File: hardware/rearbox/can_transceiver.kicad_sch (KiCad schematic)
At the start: 9 parts, among them U5 MCP2542FD

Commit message: Changed power section
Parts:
- renumbered D2 to D1, R8 to R7
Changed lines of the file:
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@@
 (kicad_sch
-	(version 20231120)
+	(version 20250114)
 	(generator "eeschema")
-	(generator_version "8.0")
+	(generator_version "9.0")
 	(paper "A4")
 	(title_block
@@
 		(shape output)
 		(at 123.19 105.41 180)
-		(fields_autoplaced yes)
 		(effects
 			(font
@@
 		(shape input)
 		(at 123.19 102.87 180)
-		(fields_autoplaced yes)
 		(effects
 			(font
@@
 		(shape bidirectional)
 		(at 177.8 118.11 0)
-		(fields_autoplaced yes)
 		(effects
 			(font
@@
 		(shape bidirectional)
 		(at 177.8 97.79 0)
-		(fields_autoplaced yes)
 		(effects
 			(font
@@
 		(on_board yes)
 		(dnp no)
-		(property "Reference" "D2"
+		(property "Reference" "D1"
 			(at 163.83 109.22 0)
 			(effects
@@
 		(dnp no)
 		(fields_autoplaced yes)
-		(property "Reference" "#FLG014"
+		(property "Reference" "#FLG012"
 			(at 149.225 81.28 0)
 			(effects
@@
 		(dnp no)
 		(fields_autoplaced yes)
-		(property "Reference" "#FLG013"
+		(property "Reference" "#FLG011"
 			(at 130.175 81.28 0)
 			(effects
@@
 		(on_board yes)
 		(dnp no)
-		(property "Reference" "R8"
+		(property "Reference" "R7"
 			(at 125.73 115.57 0)
 			(effects

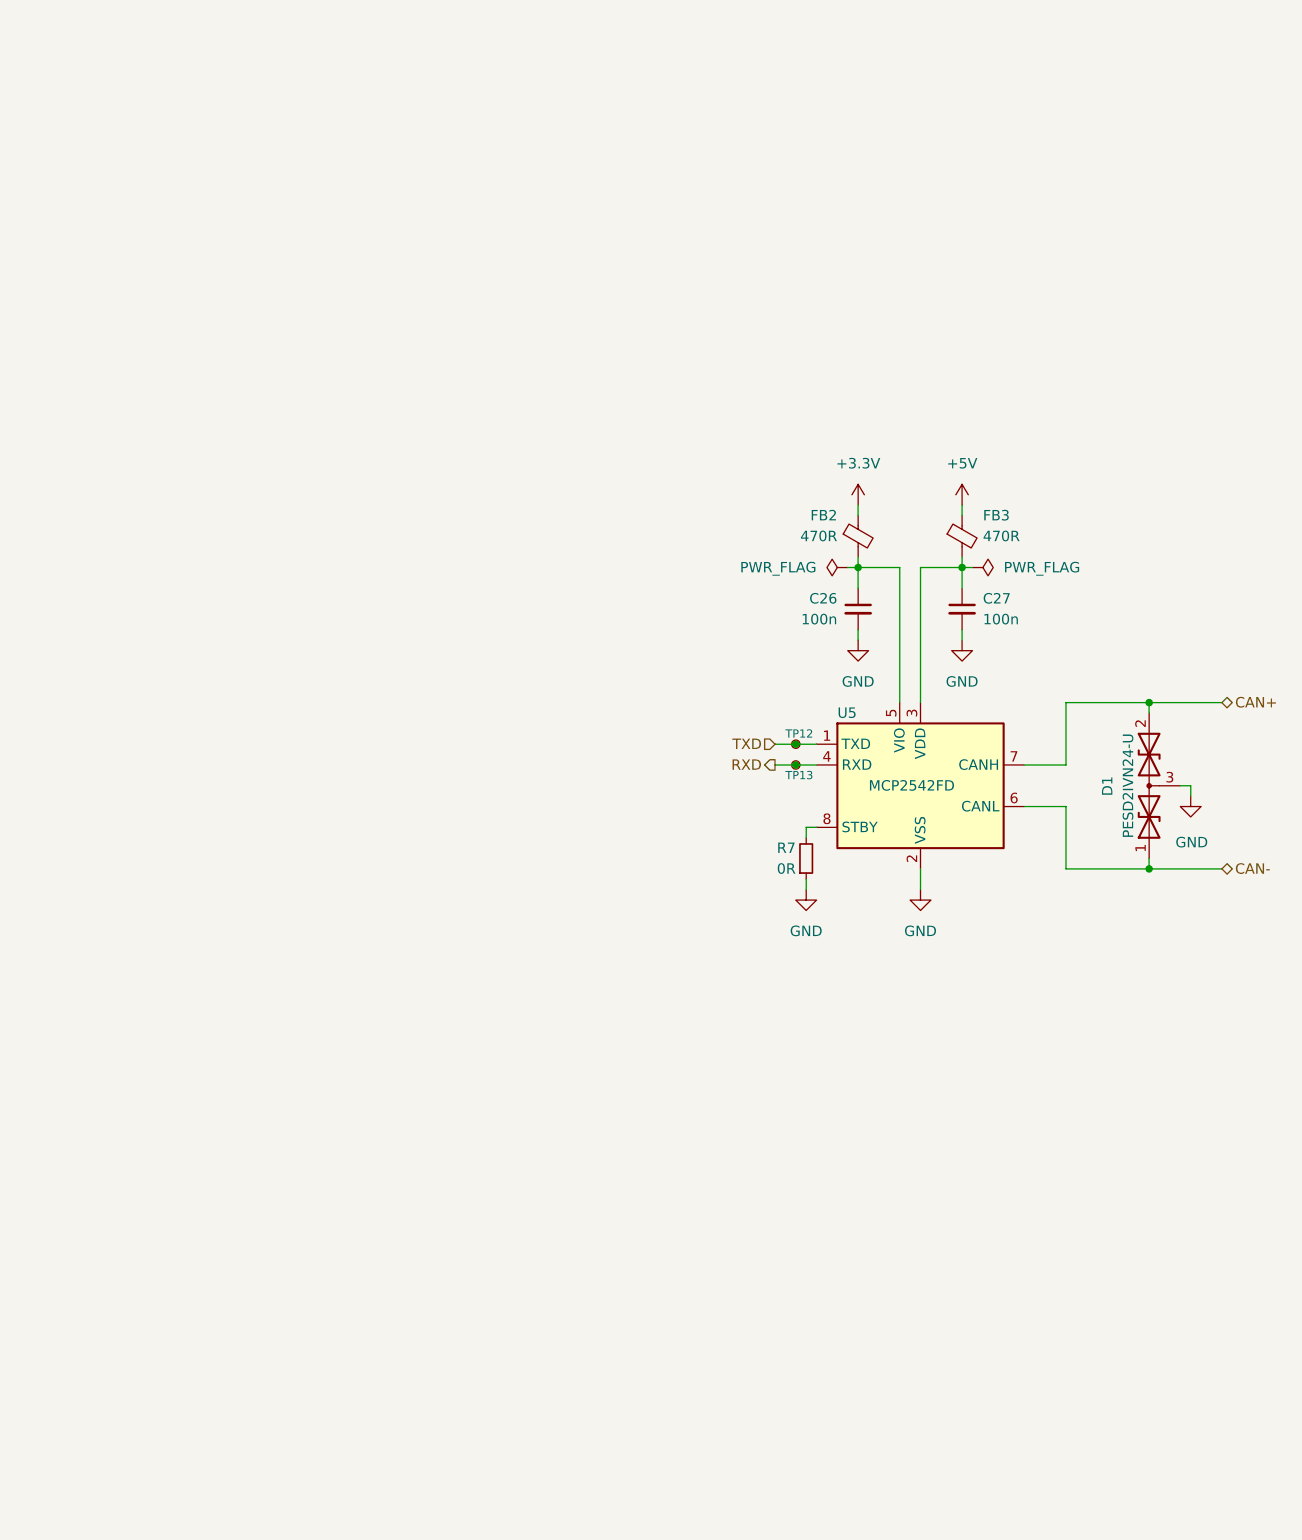
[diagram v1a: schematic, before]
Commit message: Deleted measurement systems for new iteration
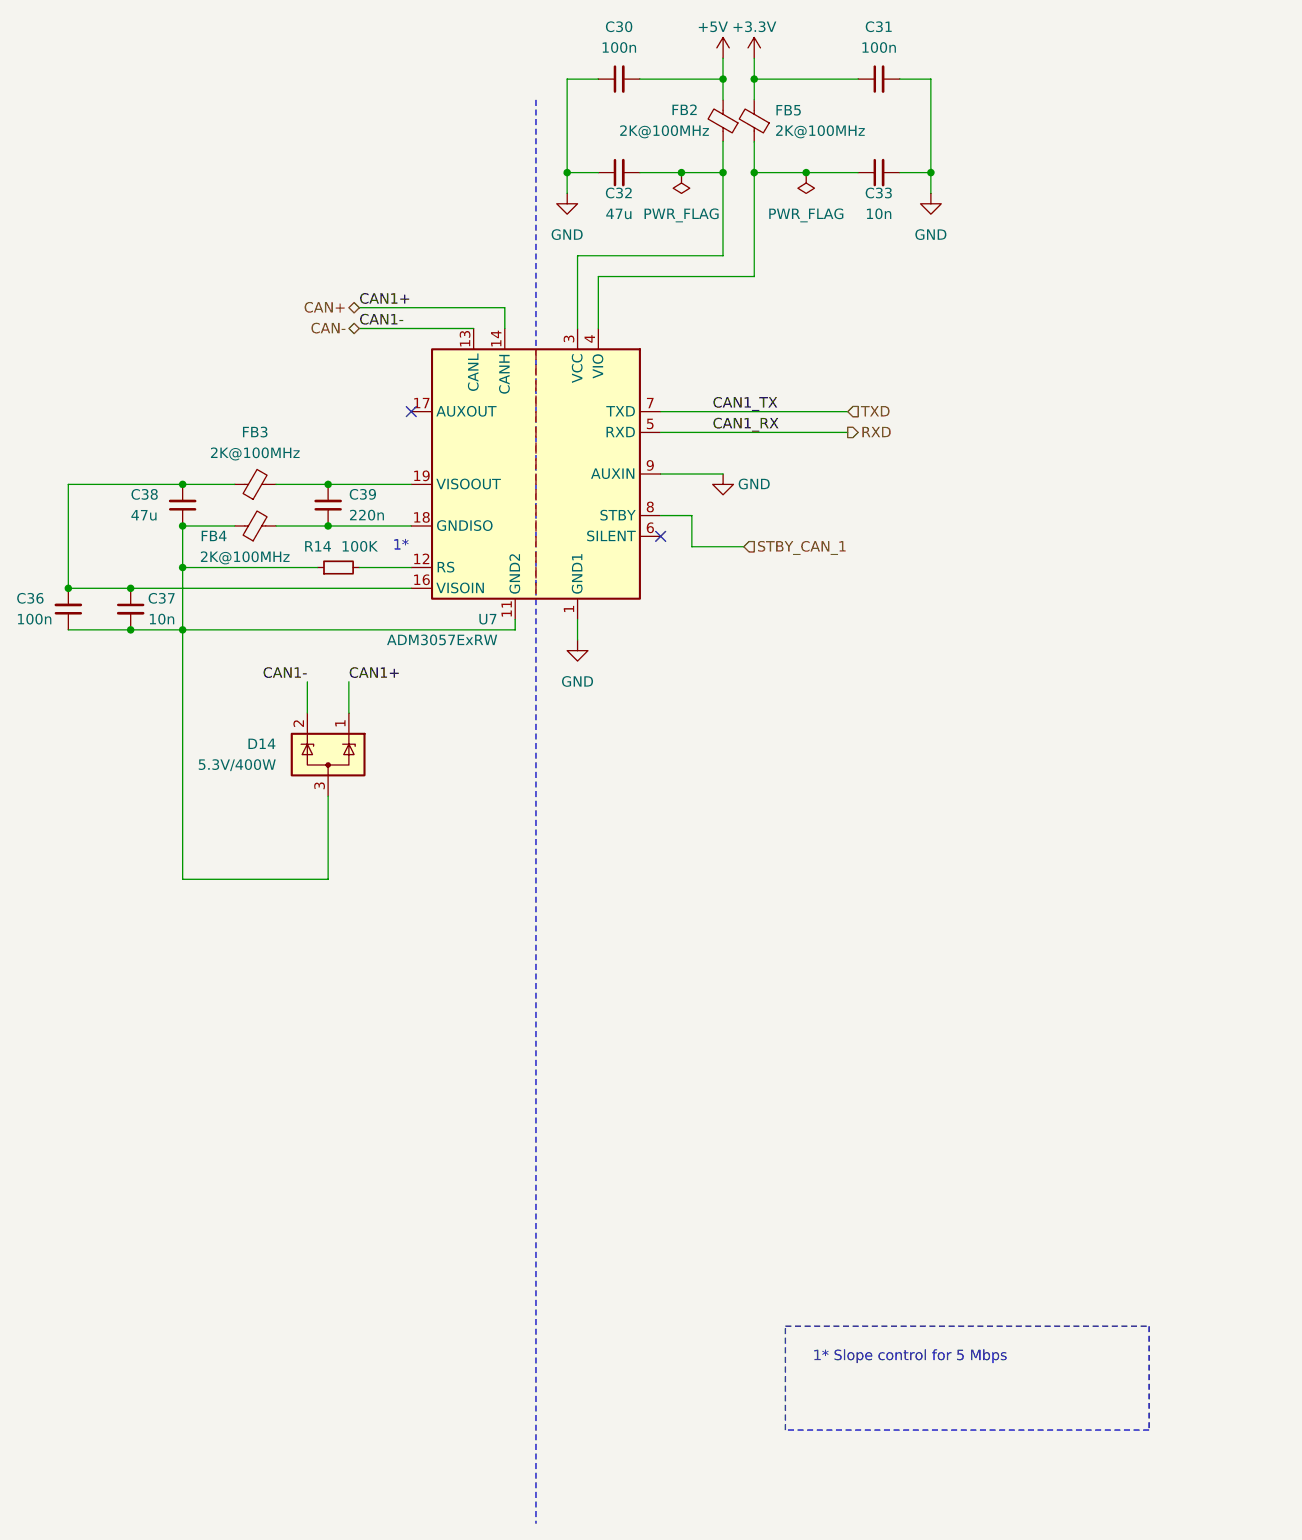
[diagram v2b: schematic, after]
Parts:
- removed C26, C27: 100n, Capacitor_SMD:C_0603_1608Metric, symbol Device:C_Small
- removed D1: PESD2IVN24-U, Package_TO_SOT_SMD:SOT-323_SC-70, symbol Device:D_TVS_Dual_AAC
- removed R7: 0R, Resistor_SMD:R_0603_1608Metric, symbol Device:R_Small
- removed TP12, TP13: TestPoint_Small, TestPoint:TestPoint_Pad_D1.0mm, symbol Connector:TestPoint_Small
- removed U5: MCP2542FD, Package_DFN_QFN:DFN-8-1EP_3x3mm_P0.65mm_EP1.55x2.4mm, symbol Interface_CAN_LIN:MCP2542FDxMF
- added C30, C31, C36: 100n, Capacitor_SMD:C_0603_1608Metric_Pad1.08x0.95mm_HandSolder, symbol Device:C_Small
- added C32, C38: 47u, Capacitor_SMD:C_0603_1608Metric_Pad1.08x0.95mm_HandSolder, symbol Device:C_Small
- added C33, C37: 10n, Capacitor_SMD:C_0603_1608Metric_Pad1.08x0.95mm_HandSolder, symbol Device:C_Small
- added C39: 220n, Capacitor_SMD:C_0603_1608Metric_Pad1.08x0.95mm_HandSolder, symbol Device:C_Small
- added D14: 5.3V/400W, Package_TO_SOT_SMD:SOT-23-3, symbol Power_Protection:ESDA5V3L
- added FB4, FB5: 2K@100MHz, Inductor_SMD:L_0603_1608Metric_Pad1.05x0.95mm_HandSolder, symbol Device:FerriteBead_Small
- added R14: 100K, Resistor_SMD:R_0603_1608Metric_Pad0.98x0.95mm_HandSolder, symbol Device:R_Small
- added U7: ADM3057ExRW, Package_SO:SOIC-20W_7.5x12.8mm_P1.27mm, symbol Interface_CAN_LIN:ADM3057ExRW
- FB2, FB3: value 470R -> 2K@100MHz; footprint Inductor_SMD:L_0603_1608Metric -> Inductor_SMD:L_0603_1608Metric_Pad1.05x0.95mm_HandSolder
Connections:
- net +3.3V: now also C31.1, FB5.2; no longer FB2.1
- net +5V: now also FB2.2, C30.2; no longer FB3.1
- net CAN+: now also D14.1 (K), U7.14 (CANH)
- net CAN-: now also D14.2 (K), U7.13 (CANL)
- net GND: now also C30.1, C31.2, C32.1, C33.2, U7.1 (GND1), U7.10 (GND1), U7.2 (GND1), U7.9 (AUXIN)
- net RXD: now also U7.5 (RXD)
- net TXD: now also U7.7 (TXD)
- net at FB3.2: now also C39.2, U7.19 (VISOOUT)
- new net: C36.1, C37.2, C38.1, D14.3 (A), FB4.1, R14.1, U7.11 (GND2), U7.15 (GND2)
- new net: C39.1, FB4.2, U7.18 (GNDISO), U7.20 (GNDISO)
- new net: C32.2, FB2.1, U7.3 (VCC)
- new net: R14.2, U7.12 (RS)
- new net: C36.2, C37.1, C38.2, FB3.1, U7.16 (VISOIN)
- new net: C33.1, FB5.1, U7.4 (VIO)
- new net STBY_CAN_1: U7.8 (STBY)
- no-connect marks 0 -> 2
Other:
- note added: "1*"
- note added: "1* Slope control for 5 Mbps"

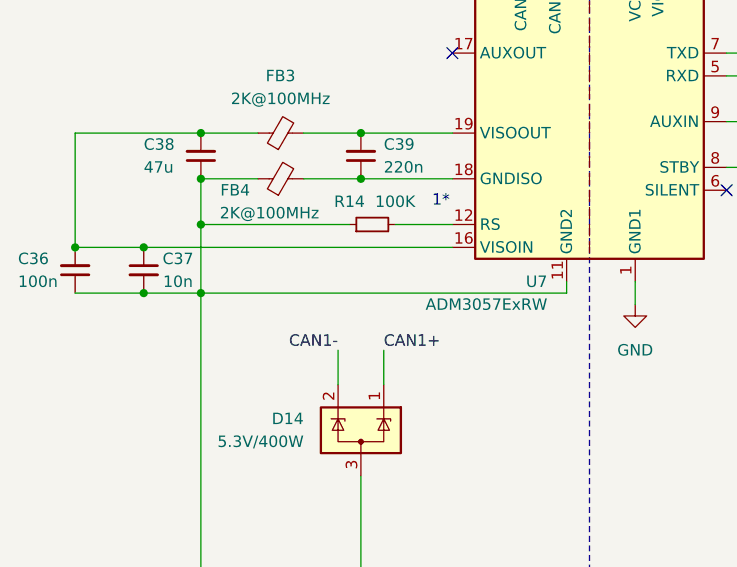
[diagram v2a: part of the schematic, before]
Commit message: Fixed badly thought out CAN GND
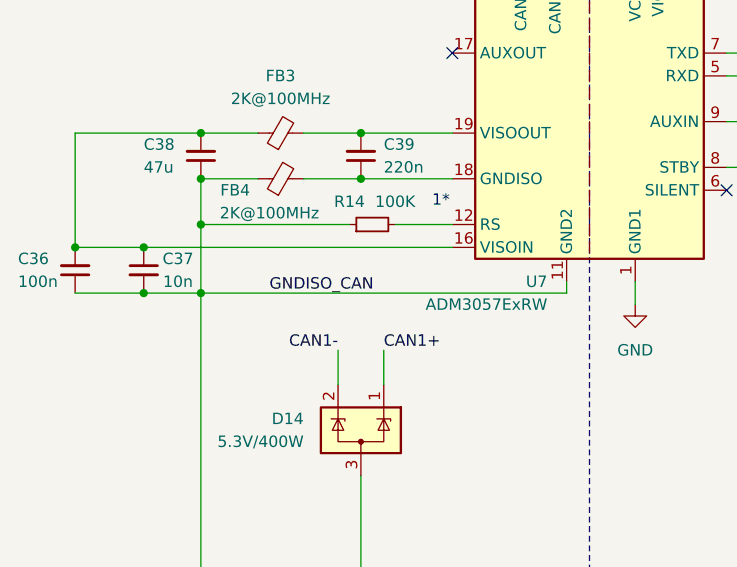
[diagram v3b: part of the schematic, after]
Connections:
- net GNDISO_CAN: now reaches C36.1, C37.2, C38.1, D14.3 (A), FB4.1, R14.1, U7.11 (GND2), U7.15 (GND2)
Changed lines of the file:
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@@
+		)
+	)
+	(label "GNDISO_CAN"
+		(at 58.42 88.9 0)
+		(effects
+			(font
+				(size 1.27 1.27)
+			)
+			(justify left bottom)
 		)
 	)

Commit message: Made ferrites into 0805's
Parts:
- FB2, FB3, FB4, FB5: footprint Inductor_SMD:L_0603_1608Metric_Pad1.05x0.95mm_HandSolder -> Inductor_SMD:L_0805_2012Metric_Pad1.05x1.20mm_HandSolder
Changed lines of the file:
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@@
 			)
 		)
-		(property "Footprint" "Inductor_SMD:L_0603_1608Metric_Pad1.05x0.95mm_HandSolder"
+		(property "Footprint" "Inductor_SMD:L_0805_2012Metric_Pad1.05x1.20mm_HandSolder"
 			(at 59.69 77.978 90)
 			(effects
@@
 			)
 		)
-		(property "Footprint" "Inductor_SMD:L_0603_1608Metric_Pad1.05x0.95mm_HandSolder"
+		(property "Footprint" "Inductor_SMD:L_0805_2012Metric_Pad1.05x1.20mm_HandSolder"
 			(at 118.618 26.67 90)
 			(effects
@@
 			)
 		)
-		(property "Footprint" "Inductor_SMD:L_0603_1608Metric_Pad1.05x0.95mm_HandSolder"
+		(property "Footprint" "Inductor_SMD:L_0805_2012Metric_Pad1.05x1.20mm_HandSolder"
 			(at 59.69 72.898 90)
 			(effects
@@
 			)
 		)
-		(property "Footprint" "Inductor_SMD:L_0603_1608Metric_Pad1.05x0.95mm_HandSolder"
+		(property "Footprint" "Inductor_SMD:L_0805_2012Metric_Pad1.05x1.20mm_HandSolder"
 			(at 122.428 26.67 90)
 			(effects
